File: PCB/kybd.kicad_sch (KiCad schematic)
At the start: 88 parts, among them J1 MJ-4PP-9, J2 Haptic Buzz, J3 lv27, SW1 SW_PUSH-MX_W_LED, SW10 SW_PUSH-MX_W_LED, SW11 SW_PUSH-MX_W_LED, SW12 SW_PUSH-MX_W_LED, SW13 SW_PUSH-MX_W_LED, SW14 SW_PUSH-MX_W_LED, SW15 SW_PUSH-MX_W_LED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

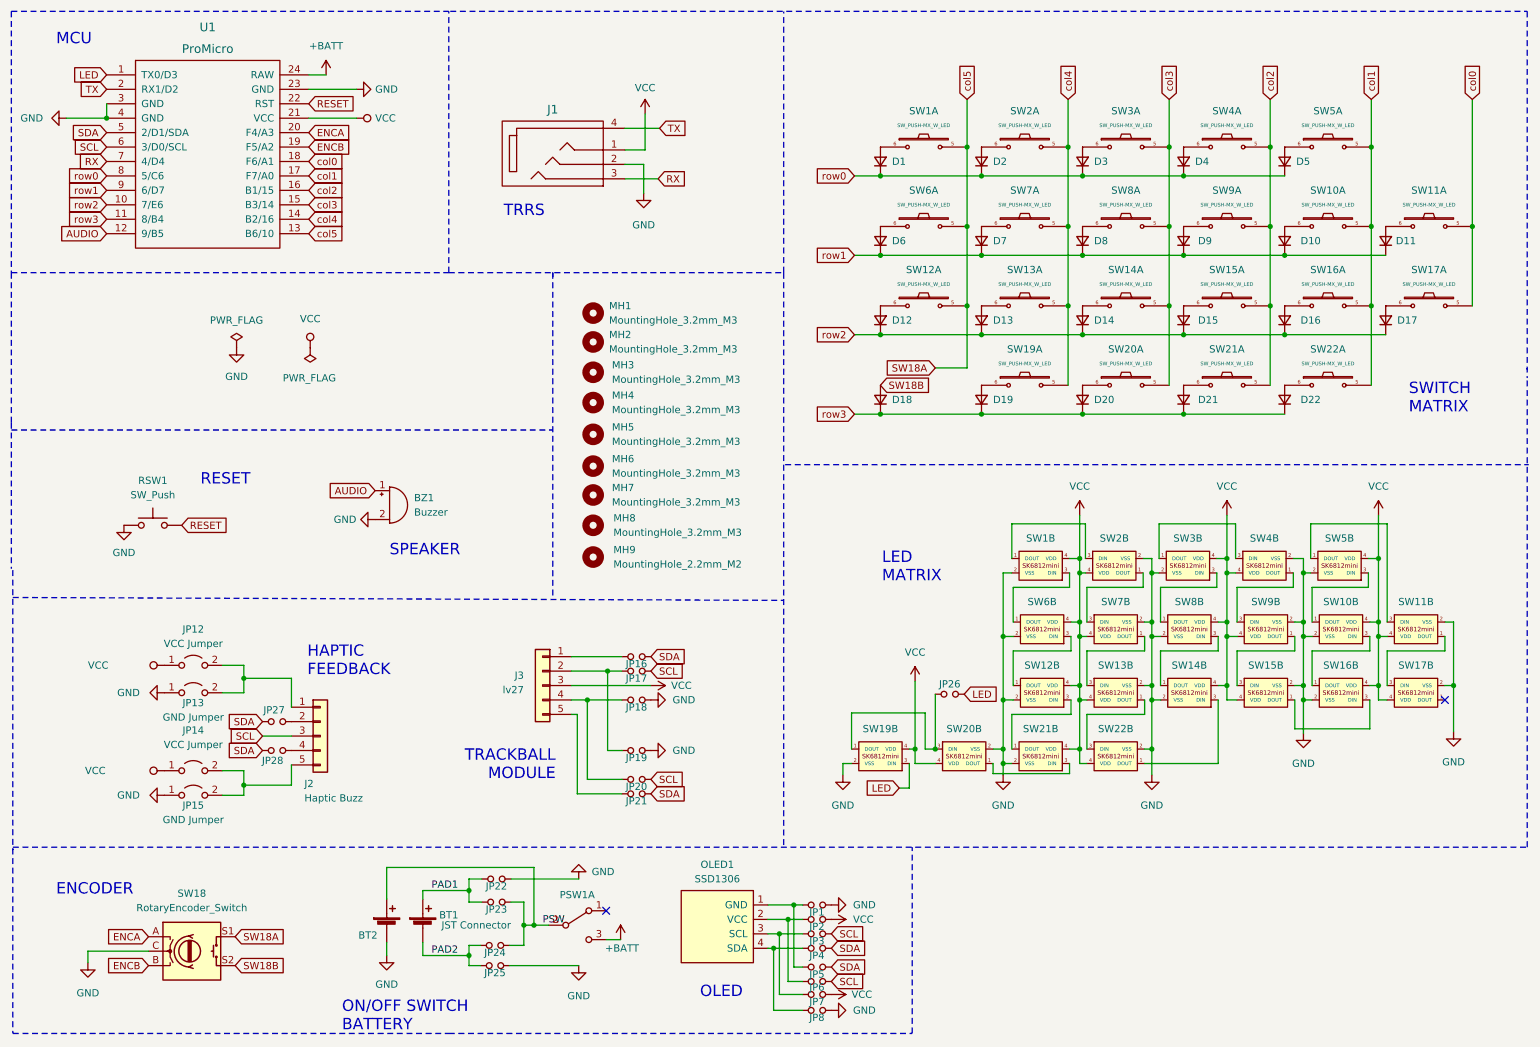
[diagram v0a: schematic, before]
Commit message: Working without power domains
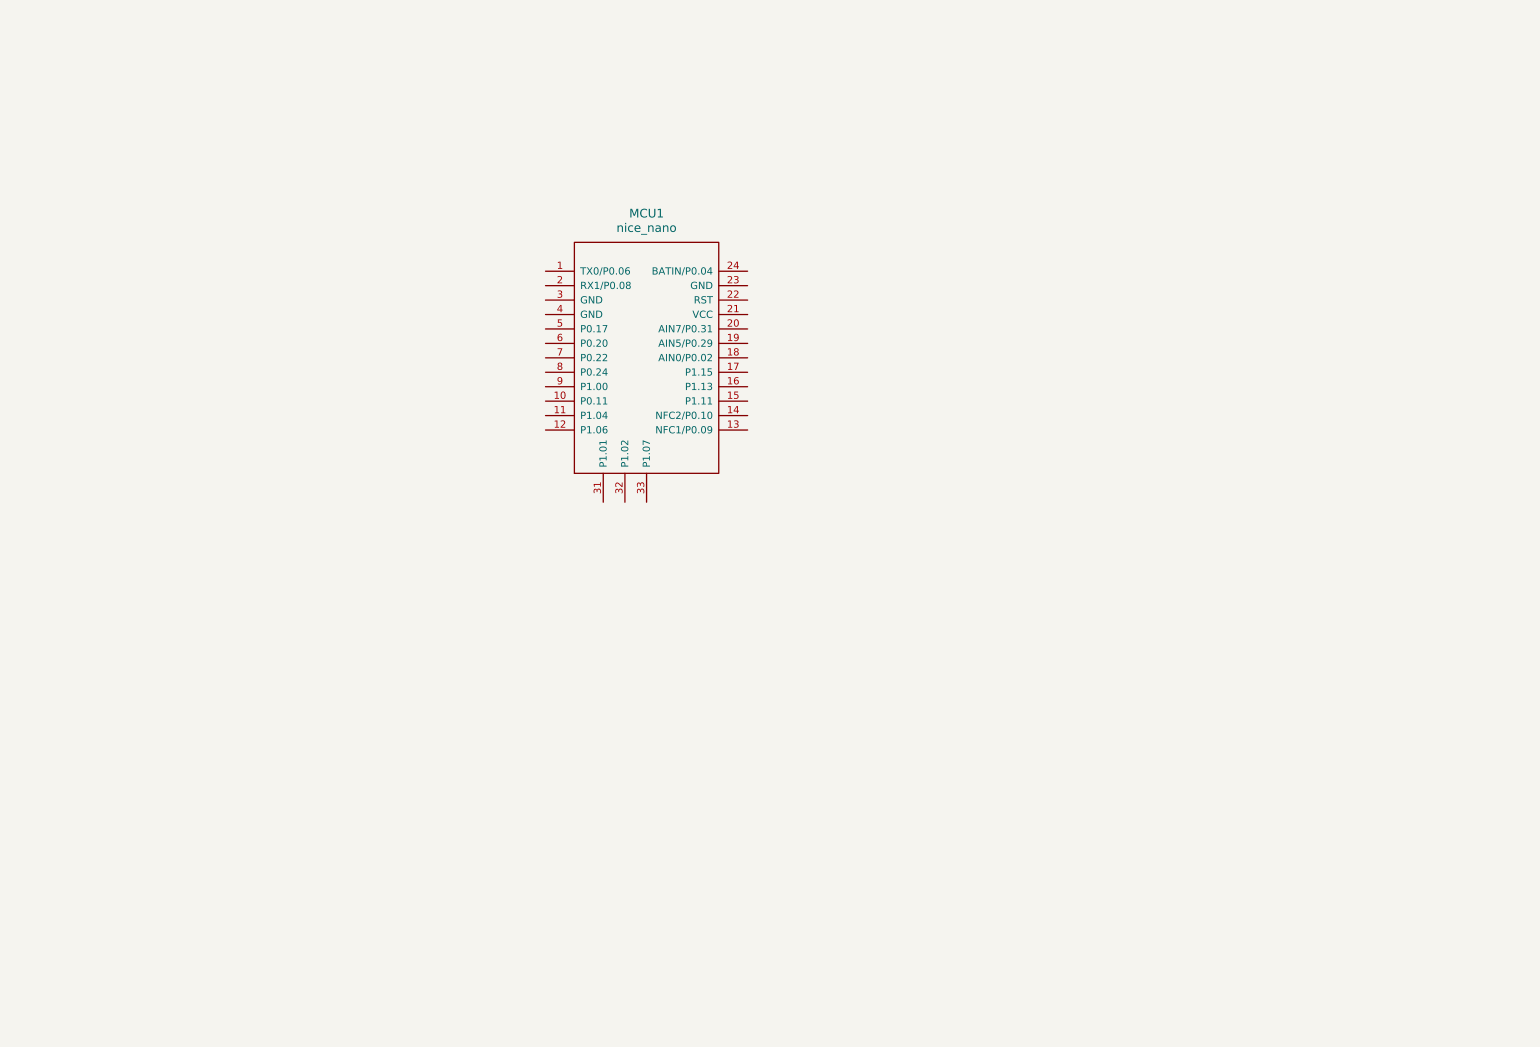
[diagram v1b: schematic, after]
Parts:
- removed BT1: JST Connector, KLOR:JST_PH_reversible, symbol Device:Battery_Cell
- removed BT2: Battery_Cell, KLOR:custombatteryconnector_small, symbol Device:Battery_Cell
- removed BZ1: Buzzer, KLOR:Buzzer_Mallory_AST1109MLTRQ_reversible, symbol Device:Buzzer
- removed D1, D10, D11, D12, D13, D14, D15, D16, D17, D18, D19, D2, D20, D21, D22, D3, D4, D5, D6, D7, D8, D9: D_Small, KLOR:Diode_SOD123, symbol Device:D_Small
- removed J1: MJ-4PP-9, KLOR:MJ-4PP-9, symbol KLORlib:MJ-4PP-9 TRRS
- removed J2: Haptic Buzz, KLOR:Pimoroni Haptic Buzz DRV2605L Driver, symbol Connector_Generic:Conn_01x05
- removed J3: lv27, KLOR:lvc27_onlyInput, symbol Connector_Generic:Conn_01x05
- removed JP1, JP16, JP17, JP18, JP19, JP2, JP21, JP22, JP23, JP24, JP25, JP26, JP27, JP28, JP3, JP4, JP5, JP6, JP7, JP8: Device_Jumper_NO_Small, KLOR:Jumper, symbol KLORlib:Device_Jumper_NO_Small
- removed JP12, JP14: VCC Jumper, KLOR:Jumper, symbol Jumper:Jumper_2_Open
- removed JP13, JP15: GND Jumper, KLOR:Jumper, symbol Jumper:Jumper_2_Open
- removed JP20: Device_Jumper_NO_Small, KLOR:Jumper, symbol SofleKeyboard-cache:Device_Jumper_NO_Small
- removed MH1, MH2, MH3, MH4, MH5, MH6, MH7, MH8: MountingHole_3.2mm_M3, MountingHole:MountingHole_3.2mm_M3, symbol Mechanical:MountingHole
- removed MH9: MountingHole_2.2mm_M2, MountingHole:MountingHole_2.2mm_M2, symbol Mechanical:MountingHole
- removed OLED1: SSD1306, KLOR:SSD1306_128x64OLED, symbol SSD1306-128x64_OLED:SSD1306
- removed PSW1: SW_DPDT_x2, KLOR:MSK12C02_reversible, symbol Switch:SW_DPDT_x2
- removed RSW1: SW_Push, KLOR:SW_Push_1P1T-MP_NO_Horizontal_Alps_SKRTLAE010_both_sides, symbol Switch:SW_Push
- removed SW1, SW10, SW11, SW12, SW13, SW14, SW15, SW16, SW17, SW19, SW2, SW20, SW21, SW22, SW3, SW4, SW5, SW6, SW7, SW8, SW9: SW_PUSH-MX_W_LED, KLOR:SK6812MINI_and_cherry, symbol KLORlib:SW_PUSH-MX_W_LED
- removed SW18: RotaryEncoder_Switch, KLOR:RotaryEncoder_Alps_EC11E-Switch_Vertical_H20mm-keebio_modified, symbol Device:RotaryEncoder_Switch
- removed U1: ProMicro, KLOR:ProMicro, symbol Buzzard:ProMicro
- added MCU1: nice_nano, symbol Nice!Nano:nice_nano
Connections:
- no-connect marks 2 -> 0
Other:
- note removed: "ENCODER"
- note removed: "HAPTIC FEEDBACK"
- note removed: "LED MATRIX"
- note removed: "MCU"
- note removed: "OLED"
- note removed: "ON/OFF SWITCH BATTERY"
- note removed: "RESET"
- note removed: "SPEAKER"
- note removed: "SWITCH MATRIX"
- note removed: "TRACKBALL MODULE"
- note removed: "TRRS"
- title: kybd Split Keyboard -> (none)
